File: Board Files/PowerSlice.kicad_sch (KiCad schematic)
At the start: 46 parts, among them J1 Conn_01x10_Pin, J2 DC_In_Barrel, J3 DC_In_Screw, J4 ESTOP, U1 PTH08080WAD, U2 PTH08080WAD, U3 INA214BIDCKR, U4 INA214BIDCKR, U5 INA214BIDCKR, U6 NUCLEO-F303K8

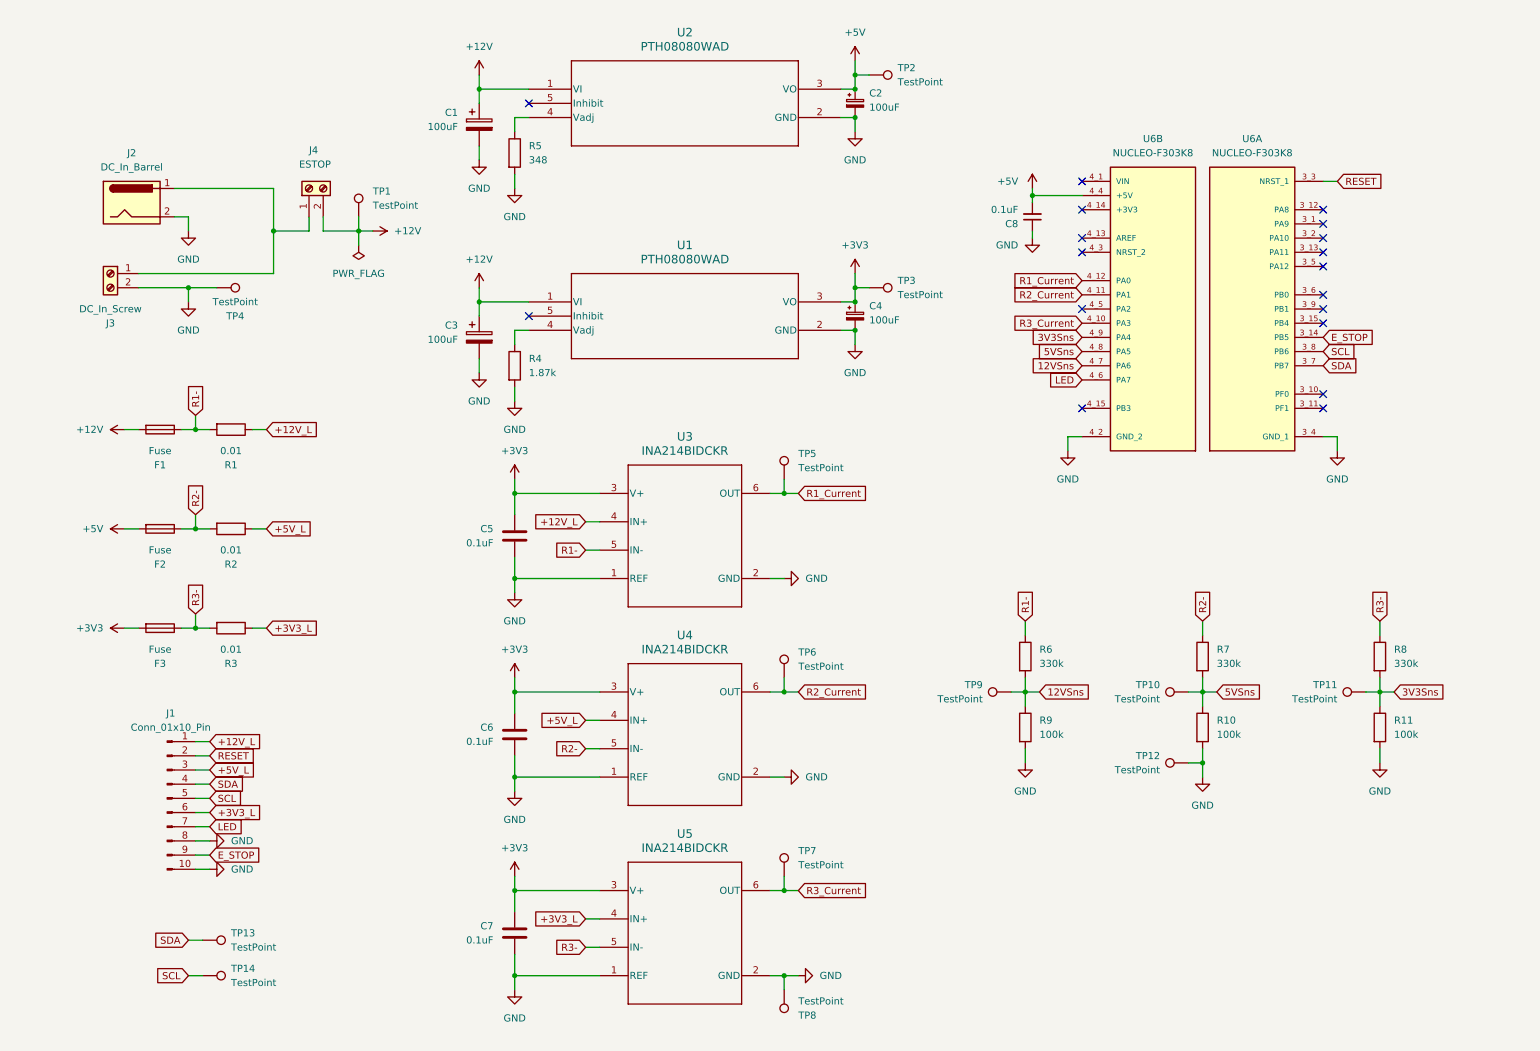
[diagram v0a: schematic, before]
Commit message: Updated to KiCAD 10, fancified schematic for final presentation, verified ERC and DRC still good
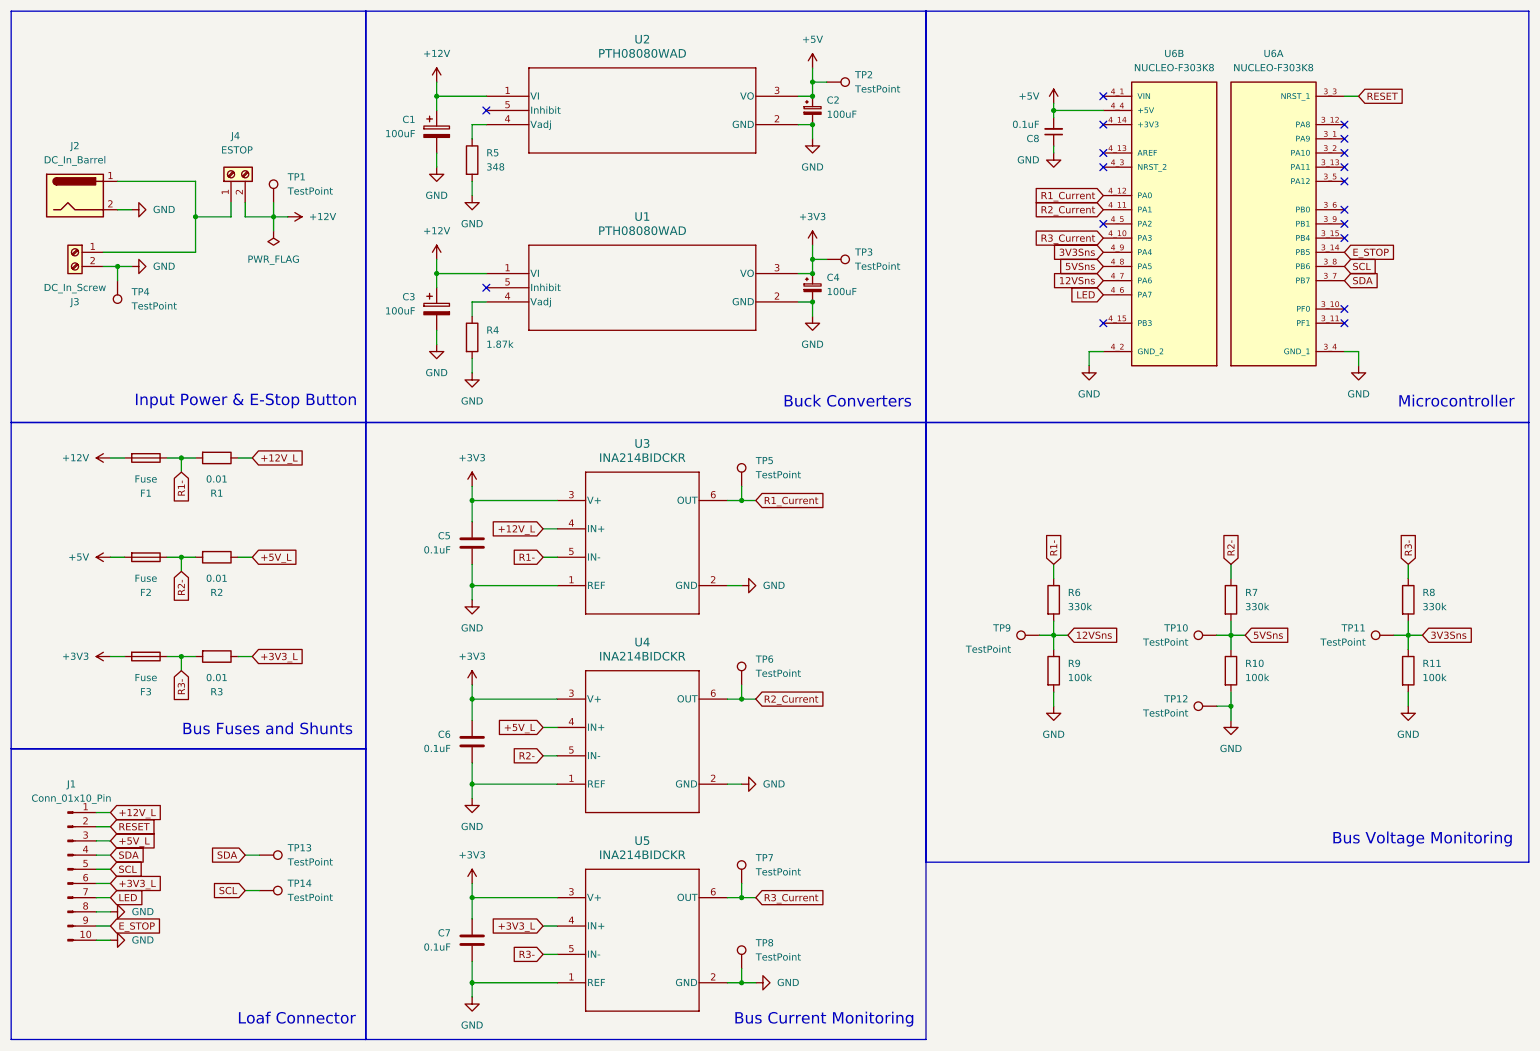
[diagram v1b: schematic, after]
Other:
- note added: "Buck Converters"
- note added: "Bus Current Monitoring"
- note added: "Bus Fuses and Shunts"
- note added: "Bus Voltage Monitoring"
- note added: "Input Power & E-Stop Button"
- note added: "Loaf Connector"
- note added: "Microcontroller"
- moved on the sheet: C1, C2, C3, C4, C5, C6, C7, C8, F1, F2, F3, J1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
